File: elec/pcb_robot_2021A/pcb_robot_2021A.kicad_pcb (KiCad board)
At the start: 2 copper layers, 39 parts, among them J1 LCD, J10 Encodeur 1, J11 Encodeur 2, J12 Conn_bat_power, J13 Tirette, J14 Couleur, J15 UART_backup, J16 Xbee, J17 PCA9685, J18 Capt_US, J19 I2C_backup, J2 IR 1.1, J20 lidar_in, J21 lidar_out, J22 Lidar_alim, J23 Galet 1.1, J24 Galet 1.2, J25 Galet 2.1, J26 Galet 2.2, J3 IR 1.2, J4 IR 1.3, J5 IR 2.1, J6 IR 2.2, J7 IR 2.3, J8 Moteur 1, J9 Moteur 2, U1 R-78E5.0-1.0, U2 Teensy3.5, U3 mosfet_lid_I1, U4 mosfet_lid_I2, U5 mosfet_lid_I3, U6 mosfet_lid_I4, U7 mosfet_lid_I5

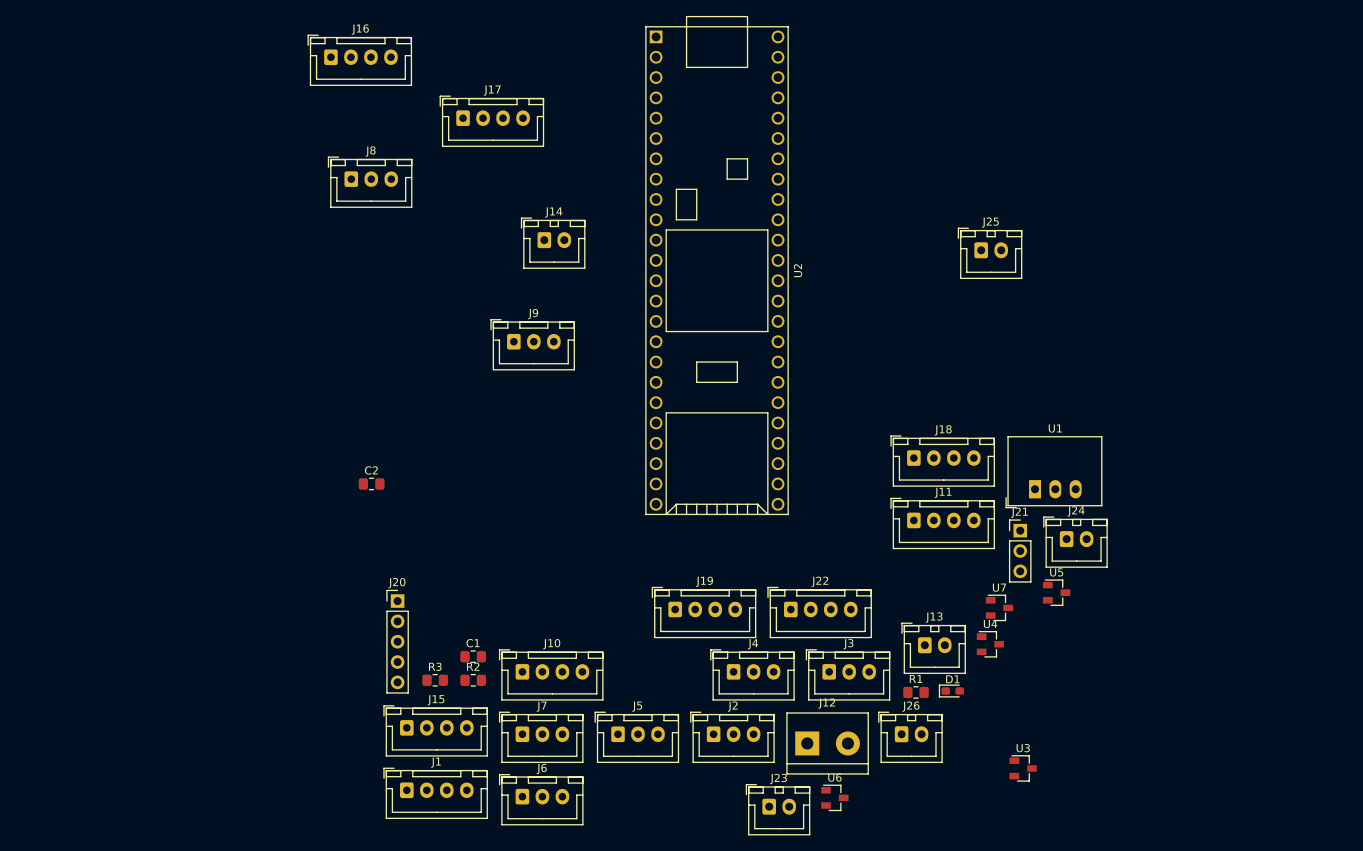
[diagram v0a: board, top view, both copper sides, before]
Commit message: positionnement item sur le pcb de main card
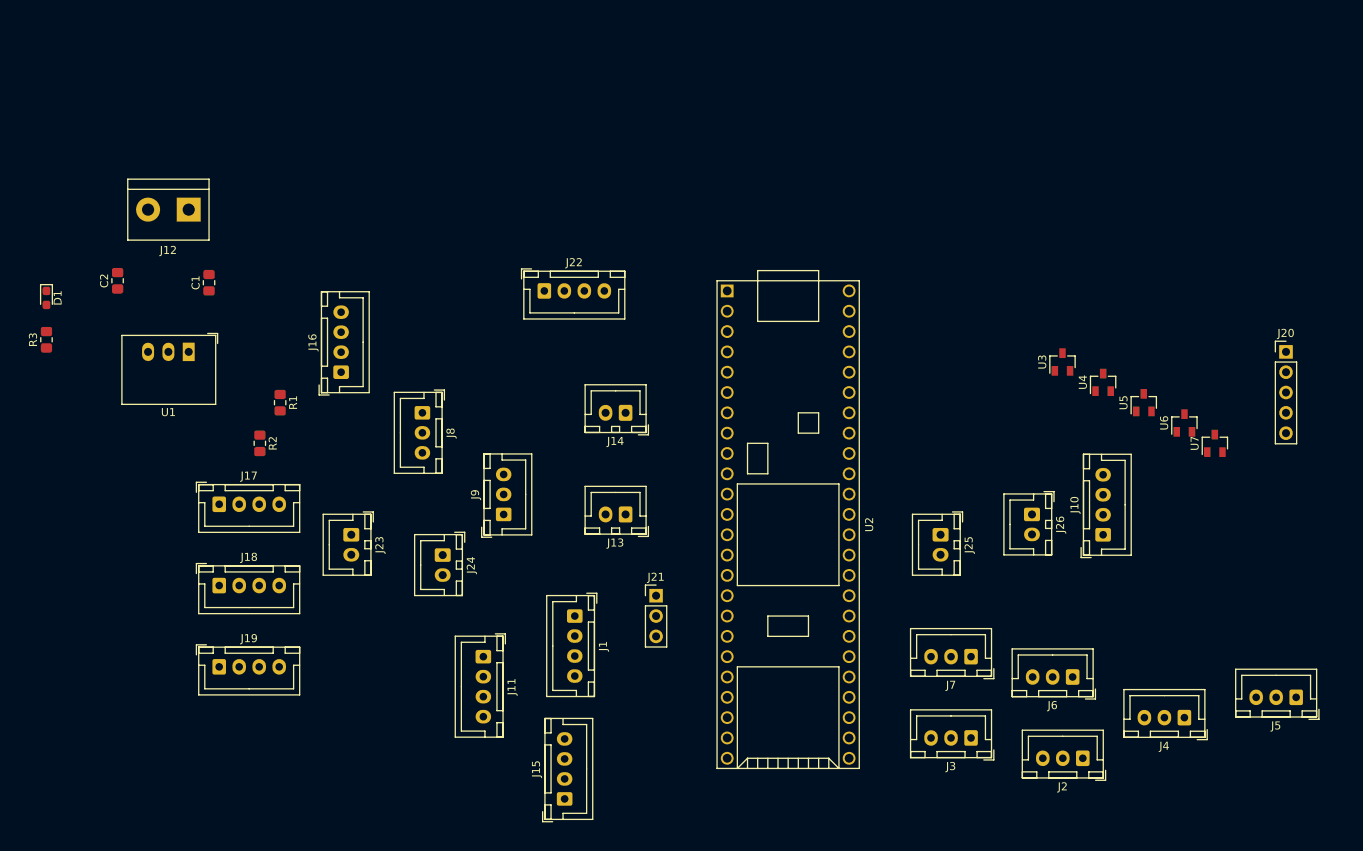
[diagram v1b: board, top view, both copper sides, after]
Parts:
- moved D1 123.5 mm to (66.0, 58.0), turned to 270 degrees
- moved J20 115.3 mm to (221.0, 64.8)
- moved U1 107.2 mm to (83.8, 64.8), turned to 180 degrees
- moved J12 102.1 mm to (83.8, 47.0), turned to 180 degrees
- moved J18 88.3 mm to (87.6, 94.0)
- moved R1 87.3 mm to (95.2, 71.1), turned to 270 degrees
- moved J5 84.9 mm to (222.2, 108.0), turned to 180 degrees
- moved J24 78.0 mm to (115.6, 90.2), turned to 270 degrees
- moved J10 74.6 mm to (198.1, 87.6), turned to 90 degrees
- moved J6 70.4 mm to (194.3, 105.4), turned to 180 degrees
- moved R3 64.6 mm to (66.0, 63.3), turned to 90 degrees
- moved U6 64.1 mm to (208.3, 73.7), turned to 90 degrees
- moved J23 62.3 mm to (104.1, 87.6), turned to 270 degrees
- moved J19 57.4 mm to (87.6, 104.1)
- moved C1 57.2 mm to (86.4, 56.1), turned to 90 degrees
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
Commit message: Fin première version routage main card
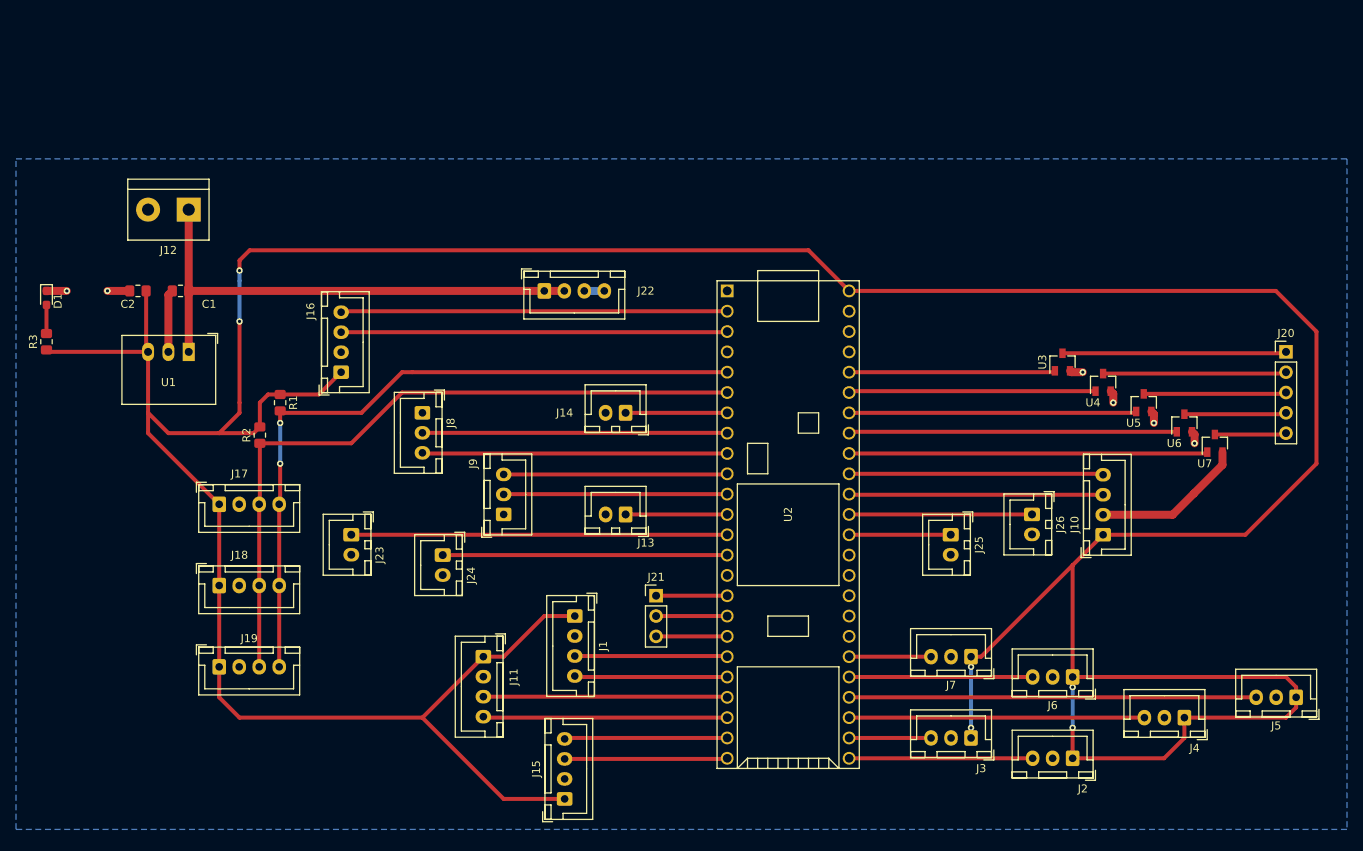
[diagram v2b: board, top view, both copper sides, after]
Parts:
- moved C1 3.71 mm to (82.8, 57.1), turned to 180 degrees
- moved C2 2.84 mm to (77.5, 57.1), turned to 180 degrees
- moved J2 1.27 mm to (194.3, 115.6)
- moved J25 1.27 mm to (179.1, 87.6)
- moved R2 1.03 mm to (92.7, 75.2), turned to 90 degrees
- moved R3 0.24 mm to (66.0, 63.5)
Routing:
- net +5V: track 0.00 -> 499.3 mm, vias 0 -> 6
- net /SCL: track 0.00 -> 90.0 mm, vias 0 -> 2
- net /SDA: track 0.00 -> 89.0 mm
- net +12V: track 0.00 -> 64.7 mm
- net /IR_out2.1: track 0.00 -> 50.9 mm
- net /Xbee_RX: track 0.00 -> 48.3 mm
- net /Xbee_TX: track 0.00 -> 48.3 mm
- net /galet_1.1: track 0.00 -> 47.0 mm
- net /lidar_in5: track 0.00 -> 44.8 mm
- net GND: track 0.00 -> 42.1 mm, vias 0 -> 6
- net /lidar_in4: track 0.00 -> 41.0 mm
- net /mot1_dir: track 0.00 -> 38.1 mm
- net /mot1_PWM: track 0.00 -> 38.1 mm
- net /IR_out1.3: track 0.00 -> 36.9 mm
- net /lidar_in3: track 0.00 -> 36.0 mm
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- added copper zone on B.Cu, net GND
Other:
- board text added: "Capteur US"
- board text added: "Carte principale"
- board text added: "Couleur"
- board text added: "Encodeur 1"
- board text added: "Encodeur 2"
- board text added: "Galet 1.1"
- board text added: "Galet 1.2"
- board text added: "Galet 2.1"
- board text added: "Galet 2.2"
- board text added: "I2C backup"
- board text added: "IR 1.1"
- board text added: "IR 1.2"
- board text added: "IR 1.3"
- board text added: "IR 2.1"
- board text added: "IR 2.2"
- board text added: "IR 2.3"
- board text added: "LCD"
- board text added: "LED bleue"
- board text added: "Lidar alim"
- board text added: "Lidar in"
- board text added: "Lidar out"
- board text added: "Moteur 1"
- board text added: "Moteur 2"
- board text added: "PCA9685"
- board text added: "R-78E5.0-1.0"
- board text added: "R1"
- board text added: "Teensy 3.5"
- board text added: "Tirette"
- board text added: "UART backup"
- board text added: "Xbee"

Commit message: Carte Principale V2 : Plus petite, correction de position de via et de connecteurs, bande plus large, ajout des trous de fixation
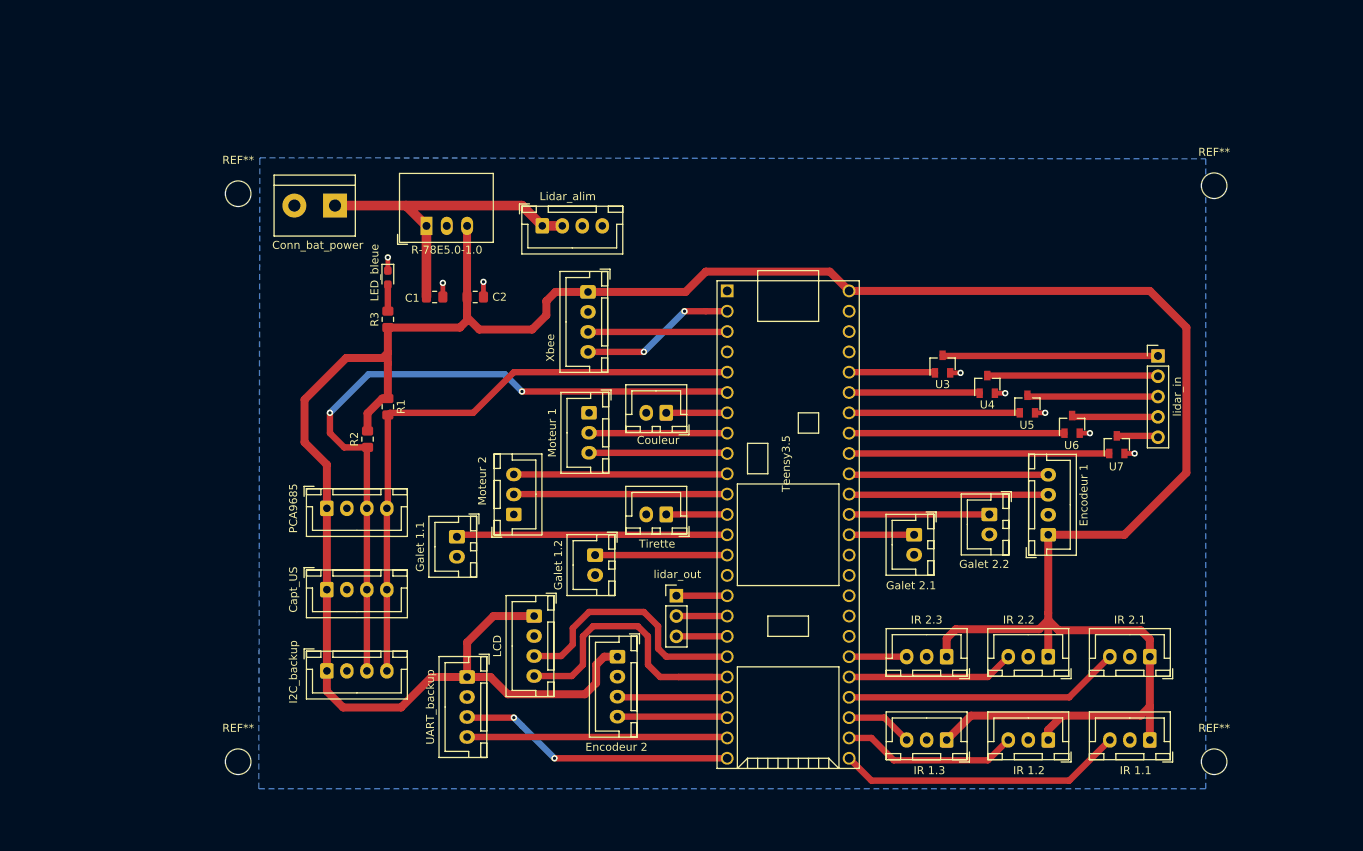
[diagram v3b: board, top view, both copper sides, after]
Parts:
- added REF**: MountingHole_3.2mm_M3, MountingHole:MountingHole_3.2mm_M3, F.Cu at (90.0, 116.0)
- added REF**: MountingHole_3.2mm_M3, MountingHole:MountingHole_3.2mm_M3, F.Cu at (90.0, 45.0)
- added REF**: MountingHole_3.2mm_M3, MountingHole:MountingHole_3.2mm_M3, F.Cu at (212.0, 44.0)
- added REF**: MountingHole_3.2mm_M3, MountingHole:MountingHole_3.2mm_M3, F.Cu at (212.0, 116.0)
- moved R3 42.8 mm to (108.7, 60.7)
- moved D1 42.7 mm to (108.7, 55.5)
- moved C2 42.2 mm to (119.6, 57.9), turned to 0 degrees
- moved U1 33.6 mm to (113.5, 49.0), turned to 0 degrees
- moved J16 32.5 mm to (133.7, 57.3), turned to 270 degrees
- moved C1 31.8 mm to (114.6, 57.9), turned to 0 degrees
- moved J4 29.8 mm to (178.6, 113.3)
- moved J8 20.8 mm to (133.9, 72.4)
- moved J15 19.5 mm to (118.6, 105.4), turned to 270 degrees
- moved J24 19.1 mm to (134.6, 90.2)
- moved J5 19.0 mm to (204.0, 102.9)
- moved J12 18.3 mm to (102.1, 46.5)
- moved J11 16.8 mm to (137.4, 102.9)
- moved J20 16.0 mm to (205.0, 65.3)
- moved U3 15.0 mm to (178.1, 66.3)
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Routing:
- net +5V: track 499.3 -> 369.0 mm, vias 6 -> 0
- net /Xbee_TX: track 48.3 -> 17.5 mm
- net GND: track 42.1 -> 11.7 mm, vias 6 -> 8
- net /Xbee_RX: track 48.3 -> 19.5 mm, vias 0 -> 2
- net /IR_out1.3: track 36.9 -> 8.35 mm
- net +12V: track 64.7 -> 41.9 mm
- net /mot1_PWM: track 38.1 -> 17.3 mm
- net /mot1_dir: track 38.1 -> 17.3 mm
- net /galet_1.2: track 35.6 -> 16.5 mm
- net /LCD_2: track 19.1 -> 37.8 mm
- net /enc2_B: track 30.5 -> 13.8 mm
- net /enc2_A: track 30.5 -> 13.9 mm
- net /IR_out2.1: track 50.9 -> 34.7 mm
- net /lidar_in1: track 25.8 -> 10.8 mm
- net /lidar_in3: track 36.0 -> 21.3 mm
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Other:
- board text added: "Robot 2021 A Carte principale"
- board text removed: "Capteur US"
- board text removed: "Carte principale"
- board text removed: "Couleur"
- board text removed: "Encodeur 1"
- board text removed: "Encodeur 2"
- board text removed: "Galet 1.1"
- board text removed: "Galet 1.2"
- board text removed: "Galet 2.1"
- board text removed: "Galet 2.2"
- board text removed: "I2C backup"
- board text removed: "IR 1.1"
- board text removed: "IR 1.2"
- board text removed: "IR 1.3"
- board text removed: "IR 2.1"
- board text removed: "IR 2.2"
- board text removed: "IR 2.3"
- board text removed: "LCD"
- board text removed: "LED bleue"
- board text removed: "Lidar alim"
- board text removed: "Lidar in"
- board text removed: "Lidar out"
- board text removed: "Moteur 1"
- board text removed: "Moteur 2"
- board text removed: "PCA9685"
- board text removed: "R-78E5.0-1.0"
- board text removed: "Teensy 3.5"
- board text removed: "Tirette"
- board text removed: "UART backup"
- board text removed: "Xbee"
